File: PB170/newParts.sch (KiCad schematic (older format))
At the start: 1 part, among them U2 74HC08

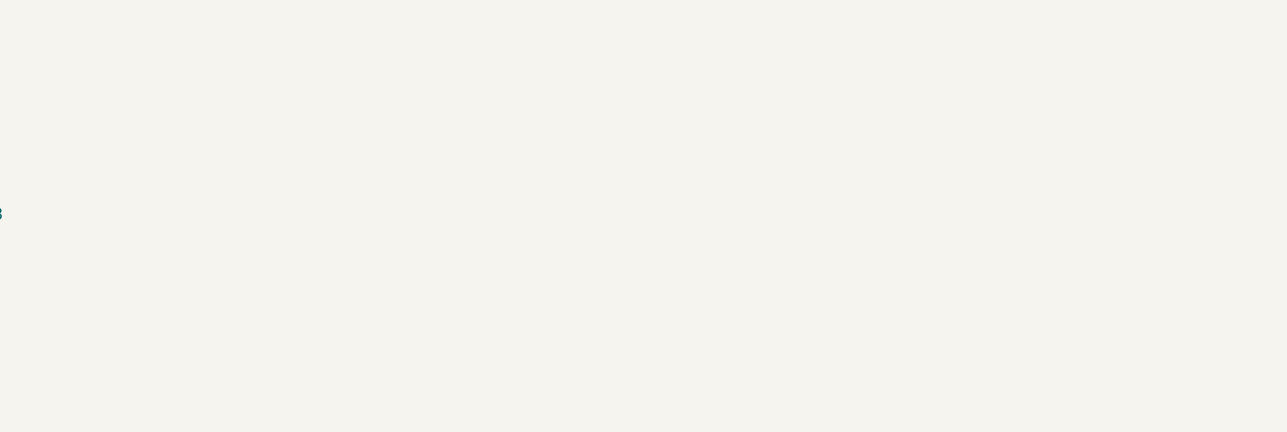
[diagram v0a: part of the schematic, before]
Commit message: Added 74HC4511D and HEF4518BT.
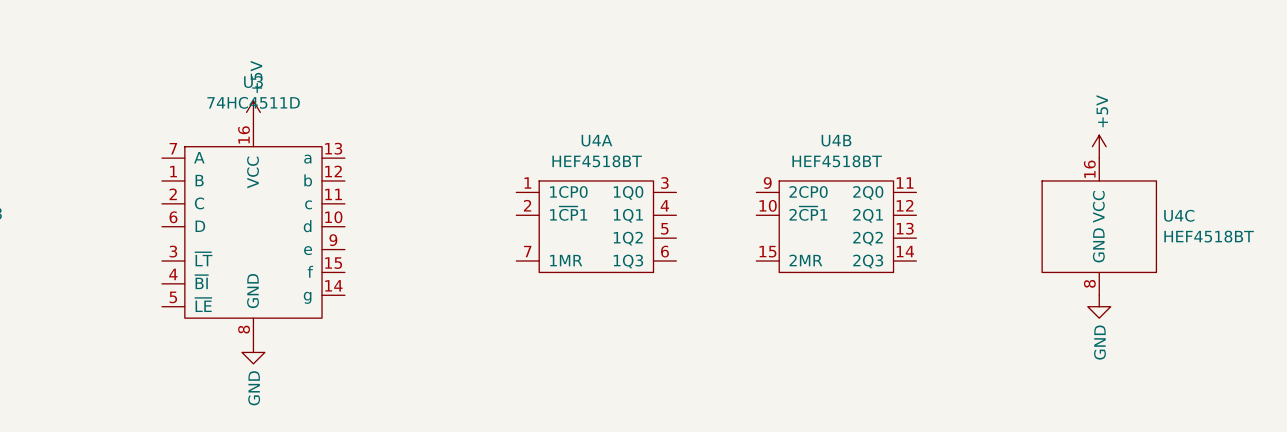
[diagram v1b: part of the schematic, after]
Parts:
- added U3: 74HC4511D, Housings_SOIC:SOIC-16_3.9x9.9mm_Pitch1.27mm, symbol PB170:74HC4511D
- added U4: HEF4518BT, Housings_SOIC:SOIC-16_3.9x9.9mm_Pitch1.27mm, symbol PB170:HEF4518BT
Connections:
- net +5V: now also U3.16 (VCC), U4.16 (VCC)
- net GND: now also U3.8 (GND), U4.8 (GND)
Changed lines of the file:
@@
+	1    0    0    -1
+$EndComp
+$Comp
+L PB170:74HC4511D U3
+U 1 1 5FE8FF7F
+P 5650 1550
+F 0 "U3" H 5650 2181 50  0000 C CNN
+F 1 "74HC4511D" H 5650 2090 50  0000 C CNN
+F 2 "Housings_SOIC:SOIC-16_3.9x9.9mm_Pitch1.27mm" H 5650 1550 50  0001 C CNN
+F 3 "https://datasheet.lcsc.com/szlcsc/Nexperia-74HC4511D-653_C87661.pdf" H 5650 1550 50  0001 C CNN
+F 4 "C87661" H 5650 1550 50  0001 C CNN "LCSC"
+	1    5650 1550
+	1    0    0    -1
+$EndComp
+$Comp
+L power:+5V #PWR?
+U 1 1 5FE90CCE
+P 5650 1100
+AR Path="/5FE90CCE" Ref="#PWR?"  Part="1"
+AR Path="/5FEB4D4D/5FE90CCE" Ref="#PWR0127"  Part="1"
+F 0 "#PWR0127" H 5650 950 50  0001 C CNN
+F 1 "+5V" V 5665 1228 50  0000 L CNN
+F 2 "" H 5650 1100 50  0001 C CNN
+F 3 "" H 5650 1100 50  0001 C CNN
+	1    5650 1100
+	1    0    0    -1
+$EndComp
+$Comp
+L power:GND #PWR?
+U 1 1 5FE91294
+P 5650 2050
+AR Path="/5FE91294" Ref="#PWR?"  Part="1"
+AR Path="/5FEB4D4D/5FE91294" Ref="#PWR0128"  Part="1"
+F 0 "#PWR0128" H 5650 1800 50  0001 C CNN
+F 1 "GND" V 5655 1922 50  0000 R CNN
+F 2 "" H 5650 2050 50  0001 C CNN
+F 3 "" H 5650 2050 50  0001 C CNN
+	1    5650 2050
+	1    0    0    -1
+$EndComp
+$Comp
+L PB170:HEF4518BT U4
+U 1 1 5FE95EE3
+P 7150 1550
+F 0 "U4" H 7150 1925 50  0000 C CNN
+F 1 "HEF4518BT" H 7150 1834 50  0000 C CNN
+F 2 "Housings_SOIC:SOIC-16_3.9x9.9mm_Pitch1.27mm" H 7150 1550 50  0001 C CNN
+F 3 "https://datasheet.lcsc.com/szlcsc/Nexperia-HEF4518BT-653_C7870.pdf" H 7150 1550 50  0001 C CNN
+F 4 "C7870" H 7150 1550 50  0001 C CNN "LCSC"
+	1    7150 1550
+	1    0    0    -1
+$EndComp
+$Comp
+L PB170:HEF4518BT U4
+U 2 1 5FE96A3D
+P 8200 1550
+F 0 "U4" H 8200 1925 50  0000 C CNN
+F 1 "HEF4518BT" H 8200 1834 50  0000 C CNN
+F 2 "Housings_SOIC:SOIC-16_3.9x9.9mm_Pitch1.27mm" H 8200 1550 50  0001 C CNN
+F 3 "https://datasheet.lcsc.com/szlcsc/Nexperia-HEF4518BT-653_C7870.pdf" H 8200 1550 50  0001 C CNN
+F 4 "C7870" H 8200 1550 50  0001 C CNN "LCSC"
+	2    8200 1550
+	1    0    0    -1
+$EndComp
+$Comp
+L PB170:HEF4518BT U4
+U 3 1 5FE96F23
+P 9350 1550
+F 0 "U4" H 9628 1596 50  0000 L CNN
+F 1 "HEF4518BT" H 9628 1505 50  0000 L CNN
+F 2 "Housings_SOIC:SOIC-16_3.9x9.9mm_Pitch1.27mm" H 9350 1550 50  0001 C CNN
+F 3 "https://datasheet.lcsc.com/szlcsc/Nexperia-HEF4518BT-653_C7870.pdf" H 9350 1550 50  0001 C CNN
+F 4 "C7870" H 9350 1550 50  0001 C CNN "LCSC"
+	3    9350 1550
+	1    0    0    -1
+$EndComp
+$Comp
+L power:+5V #PWR?
+U 1 1 5FE97657
+P 9350 1250
+AR Path="/5FE97657" Ref="#PWR?"  Part="1"
+AR Path="/5FEB4D4D/5FE97657" Ref="#PWR0129"  Part="1"
+F 0 "#PWR0129" H 9350 1100 50  0001 C CNN
+F 1 "+5V" V 9365 1378 50  0000 L CNN
+F 2 "" H 9350 1250 50  0001 C CNN
+F 3 "" H 9350 1250 50  0001 C CNN
+	1    9350 1250
+	1    0    0    -1
+$EndComp
+$Comp
+L power:GND #PWR?
+U 1 1 5FE97C84
+P 9350 1850
+AR Path="/5FE97C84" Ref="#PWR?"  Part="1"
+AR Path="/5FEB4D4D/5FE97C84" Ref="#PWR0130"  Part="1"
+F 0 "#PWR0130" H 9350 1600 50  0001 C CNN
+F 1 "GND" V 9355 1722 50  0000 R CNN
+F 2 "" H 9350 1850 50  0001 C CNN
+F 3 "" H 9350 1850 50  0001 C CNN
+	1    9350 1850
 	1    0    0    -1
 $EndComp

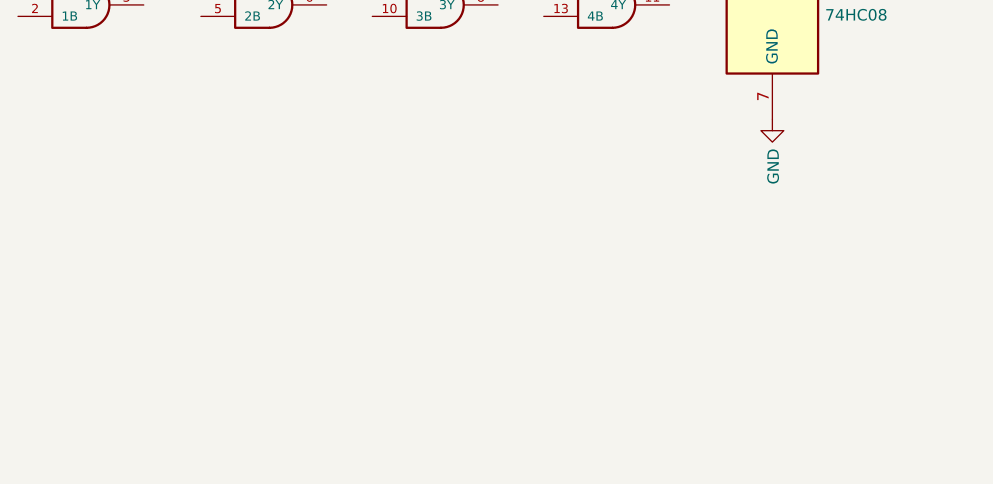
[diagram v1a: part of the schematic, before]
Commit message: Added sample OR gate 74HC32.
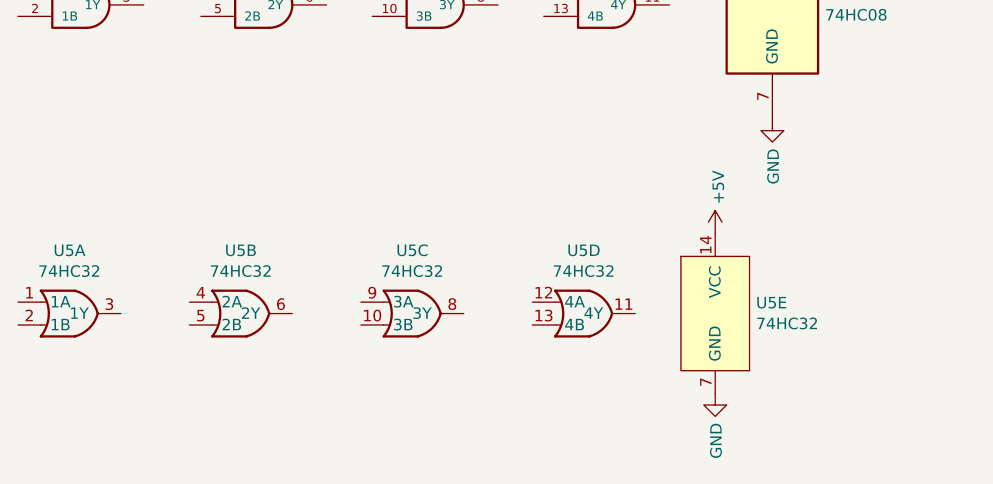
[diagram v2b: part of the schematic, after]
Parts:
- added U5: 74HC32, Housings_SOIC:SOIC-14_3.9x8.7mm_Pitch1.27mm, symbol PB170:74HC32
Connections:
- net +5V: now also U5.14 (VCC)
- net GND: now also U5.7 (GND)
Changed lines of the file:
@@
+	1    0    0    -1
+$EndComp
+$Comp
+L PB170:74HC32 U5
+U 1 1 6002CB84
+P 1000 2800
+F 0 "U5" H 975 3075 50  0000 C CNN
+F 1 "74HC32" H 975 2984 50  0000 C CNN
+F 2 "Housings_SOIC:SOIC-14_3.9x8.7mm_Pitch1.27mm" H 450 3000 50  0001 C CNN
+F 3 "https://datasheet.lcsc.com/szlcsc/Nexperia-74HC32D-653_C5632.pdf" H 450 3000 50  0001 C CNN
+F 4 "C5632" H 1000 2800 50  0001 C CNN "LCSC"
+	1    1000 2800
+	1    0    0    -1
+$EndComp
+$Comp
+L PB170:74HC32 U5
+U 2 1 6002F342
+P 1750 2800
+F 0 "U5" H 1725 3075 50  0000 C CNN
+F 1 "74HC32" H 1725 2984 50  0000 C CNN
+F 2 "Housings_SOIC:SOIC-14_3.9x8.7mm_Pitch1.27mm" H 1200 3000 50  0001 C CNN
+F 3 "https://datasheet.lcsc.com/szlcsc/Nexperia-74HC32D-653_C5632.pdf" H 1200 3000 50  0001 C CNN
+F 4 "C5632" H 1750 2800 50  0001 C CNN "LCSC"
+	2    1750 2800
+	1    0    0    -1
+$EndComp
+$Comp
+L PB170:74HC32 U5
+U 3 1 6003083A
+P 2500 2800
+F 0 "U5" H 2475 3075 50  0000 C CNN
+F 1 "74HC32" H 2475 2984 50  0000 C CNN
+F 2 "Housings_SOIC:SOIC-14_3.9x8.7mm_Pitch1.27mm" H 1950 3000 50  0001 C CNN
+F 3 "https://datasheet.lcsc.com/szlcsc/Nexperia-74HC32D-653_C5632.pdf" H 1950 3000 50  0001 C CNN
+F 4 "C5632" H 2500 2800 50  0001 C CNN "LCSC"
+	3    2500 2800
+	1    0    0    -1
+$EndComp
+$Comp
+L PB170:74HC32 U5
+U 4 1 60030FE6
+P 3250 2800
+F 0 "U5" H 3225 3075 50  0000 C CNN
+F 1 "74HC32" H 3225 2984 50  0000 C CNN
+F 2 "Housings_SOIC:SOIC-14_3.9x8.7mm_Pitch1.27mm" H 2700 3000 50  0001 C CNN
+F 3 "https://datasheet.lcsc.com/szlcsc/Nexperia-74HC32D-653_C5632.pdf" H 2700 3000 50  0001 C CNN
+F 4 "C5632" H 3250 2800 50  0001 C CNN "LCSC"
+	4    3250 2800
+	1    0    0    -1
+$EndComp
+$Comp
+L PB170:74HC32 U5
+U 5 1 60031D42
+P 4100 2800
+F 0 "U5" H 3978 2846 50  0000 L CNN
+F 1 "74HC32" H 3978 2755 50  0000 L CNN
+F 2 "Housings_SOIC:SOIC-14_3.9x8.7mm_Pitch1.27mm" H 3550 3000 50  0001 C CNN
+F 3 "https://datasheet.lcsc.com/szlcsc/Nexperia-74HC32D-653_C5632.pdf" H 3550 3000 50  0001 C CNN
+F 4 "C5632" H 4100 2800 50  0001 C CNN "LCSC"
+	5    4100 2800
+	1    0    0    -1
+$EndComp
+$Comp
+L power:GND #PWR?
+U 1 1 600397BF
+P 3800 3150
+AR Path="/600397BF" Ref="#PWR?"  Part="1"
+AR Path="/5FEB4D4D/600397BF" Ref="#PWR0131"  Part="1"
+F 0 "#PWR0131" H 3800 2900 50  0001 C CNN
+F 1 "GND" V 3805 3022 50  0000 R CNN
+F 2 "" H 3800 3150 50  0001 C CNN
+F 3 "" H 3800 3150 50  0001 C CNN
+	1    3800 3150
+	1    0    0    -1
+$EndComp
+$Comp
+L power:+5V #PWR?
+U 1 1 60039BCC
+P 3800 2450
+AR Path="/60039BCC" Ref="#PWR?"  Part="1"
+AR Path="/5FEB4D4D/60039BCC" Ref="#PWR0132"  Part="1"
+F 0 "#PWR0132" H 3800 2300 50  0001 C CNN
+F 1 "+5V" V 3815 2578 50  0000 L CNN
+F 2 "" H 3800 2450 50  0001 C CNN
+F 3 "" H 3800 2450 50  0001 C CNN
+	1    3800 2450
 	1    0    0    -1
 $EndComp

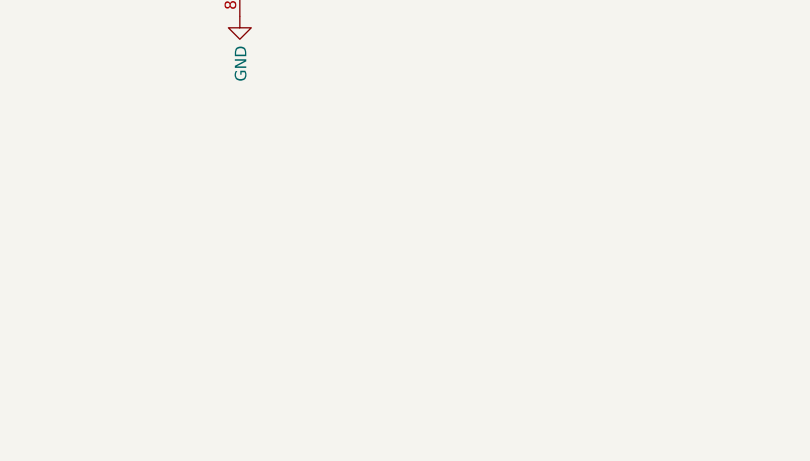
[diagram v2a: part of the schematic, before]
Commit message: Created examples with new THT parts.
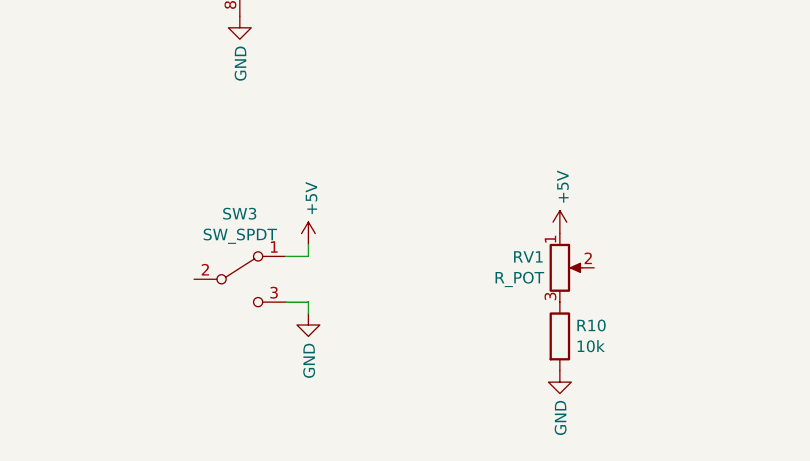
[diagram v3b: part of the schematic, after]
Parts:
- added R10: 10k, Resistor_SMD:R_0603_1608Metric, symbol Device:R
- added RV1: R_POT, PB170:potentiometer10k, symbol Device:R_POT
- added SW3: SW_SPDT, PB170:toggleSwitch, symbol Switch:SW_SPDT
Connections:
- net +5V: now also RV1.1, SW3.1 (A)
- net GND: now also R10.2, SW3.3 (C)
- new net: R10.1, RV1.3
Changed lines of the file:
@@
 	1    0    0    -1
 $EndComp
+$Comp
+L Switch:SW_SPDT SW3
+U 1 1 601DAABB
+P 5650 3200
+F 0 "SW3" H 5650 3485 50  0000 C CNN
+F 1 "SW_SPDT" H 5650 3394 50  0000 C CNN
+F 2 "PB170:toggleSwitch" H 5650 3200 50  0001 C CNN
+F 3 "https://datasheet.lcsc.com/szlcsc/1809140824_Korean-Hroparts-Elec-SS-12F44-G5_C136718.pdf" H 5650 3200 50  0001 C CNN
+F 4 "C136718" H 5650 3200 50  0001 C CNN "LCSC"
+	1    5650 3200
+	1    0    0    -1
+$EndComp
+$Comp
+L Device:R_POT RV1
+U 1 1 601DBB34
+P 7050 3150
+F 0 "RV1" H 6981 3196 50  0000 R CNN
+F 1 "R_POT" H 6981 3105 50  0000 R CNN
+F 2 "PB170:potentiometer10k" H 7050 3150 50  0001 C CNN
+F 3 "https://datasheet.lcsc.com/szlcsc/1810170732_Nidec-Copal-Elec-ST-4EA-10K-ohm-103_C132879.pdf" H 7050 3150 50  0001 C CNN
+F 4 "C132879" H 7050 3150 50  0001 C CNN "LCSC"
+	1    7050 3150
+	1    0    0    -1
+$EndComp
+$Comp
+L Device:R R?
+U 1 1 601EAE8F
+P 7050 3450
+AR Path="/601EAE8F" Ref="R?"  Part="1"
+AR Path="/5FEB4D4D/601EAE8F" Ref="R10"  Part="1"
+F 0 "R10" H 7120 3496 50  0000 L CNN
+F 1 "10k" H 7120 3405 50  0000 L CNN
+F 2 "Resistor_SMD:R_0603_1608Metric" V 6980 3450 50  0001 C CNN
+F 3 "https://datasheet.lcsc.com/szlcsc/Uniroyal-Elec-0603WAF1002T5E_C25804.pdf" H 7050 3450 50  0001 C CNN
+F 4 "C25804" H 7050 3450 50  0001 C CNN "LCSC"
+	1    7050 3450
+	1    0    0    -1
+$EndComp
+$Comp
+L power:GND #PWR?
+U 1 1 601EB635
+P 7050 3600
+AR Path="/601EB635" Ref="#PWR?"  Part="1"
+AR Path="/5FEB4D4D/601EB635" Ref="#PWR0123"  Part="1"
+F 0 "#PWR0123" H 7050 3350 50  0001 C CNN
+F 1 "GND" V 7055 3472 50  0000 R CNN
+F 2 "" H 7050 3600 50  0001 C CNN
+F 3 "" H 7050 3600 50  0001 C CNN
+	1    7050 3600
+	1    0    0    -1
+$EndComp
+$Comp
+L power:+5V #PWR?
+U 1 1 601EBDCA
+P 7050 3000
+AR Path="/601EBDCA" Ref="#PWR?"  Part="1"
+AR Path="/5FEB4D4D/601EBDCA" Ref="#PWR0124"  Part="1"
+F 0 "#PWR0124" H 7050 2850 50  0001 C CNN
+F 1 "+5V" V 7065 3128 50  0000 L CNN
+F 2 "" H 7050 3000 50  0001 C CNN
+F 3 "" H 7050 3000 50  0001 C CNN
+	1    7050 3000
+	1    0    0    -1
+$EndComp
+$Comp
+L power:+5V #PWR?
+U 1 1 601ECB0F
+P 5950 3050
+AR Path="/601ECB0F" Ref="#PWR?"  Part="1"
+AR Path="/5FEB4D4D/601ECB0F" Ref="#PWR0133"  Part="1"
+F 0 "#PWR0133" H 5950 2900 50  0001 C CNN
+F 1 "+5V" V 5965 3178 50  0000 L CNN
+F 2 "" H 5950 3050 50  0001 C CNN
+F 3 "" H 5950 3050 50  0001 C CNN
+	1    5950 3050
+	1    0    0    -1
+$EndComp
+$Comp
+L power:GND #PWR?
+U 1 1 601ED3E5
+P 5950 3350
+AR Path="/601ED3E5" Ref="#PWR?"  Part="1"
+AR Path="/5FEB4D4D/601ED3E5" Ref="#PWR0134"  Part="1"
+F 0 "#PWR0134" H 5950 3100 50  0001 C CNN
+F 1 "GND" V 5955 3222 50  0000 R CNN
+F 2 "" H 5950 3350 50  0001 C CNN
+F 3 "" H 5950 3350 50  0001 C CNN
+	1    5950 3350
+	1    0    0    -1
+$EndComp
+Wire Wire Line
+	5850 3300 5950 3300
+Wire Wire Line
+	5950 3300 5950 3350
+Wire Wire Line
+	5850 3100 5950 3100
+Wire Wire Line
+	5950 3100 5950 3050
 $EndSCHEMATC
